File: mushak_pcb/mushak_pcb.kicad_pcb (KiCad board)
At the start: 4 copper layers, 45.8 x 40 mm, 110 parts, among them IC1 AS5600-ASOT, IC2 AS5600-ASOT, J1 Conn_01x04_Male, J10 IR_1, J11 AS5600_1, J12 IR_2, J13 AS5600_2, J14 IR_3, J15 ToF, J16 IR_4, J17 ToF, J2 Conn_01x02_Female, J3 BLE_Conn, J4 AS5600_Left, J5 AS5600_Right, J6 IR_1, J7 IR_3, J8 IR_2, J9 IR_4, M1 motor, M2 motor, Q1 DMN3065LW-7, Q2 DMN3065LW-7, Q3 DMN3065LW-7, Q4 DMN3065LW-7, Q5 DMN3065LW-7, SW1 SW_Push, SW2 SW_Push, U2 TLV1117LV30DCYT, U3 DRV8833PW, U4 VL6180XV0NR/1, U5 MPU-6500, U6 STM32F405RGTx, Y1 25Mhz, Y2 32.769kHz

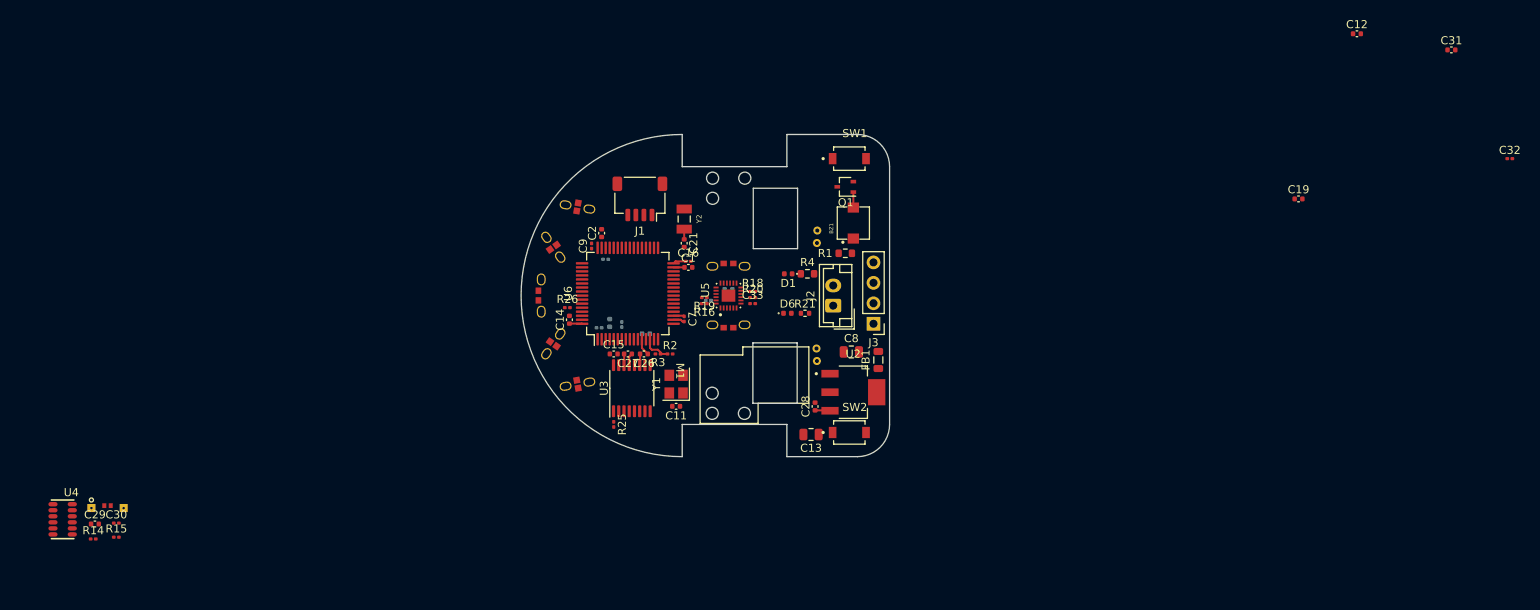
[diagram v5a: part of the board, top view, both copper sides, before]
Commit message: VL6180x part routed
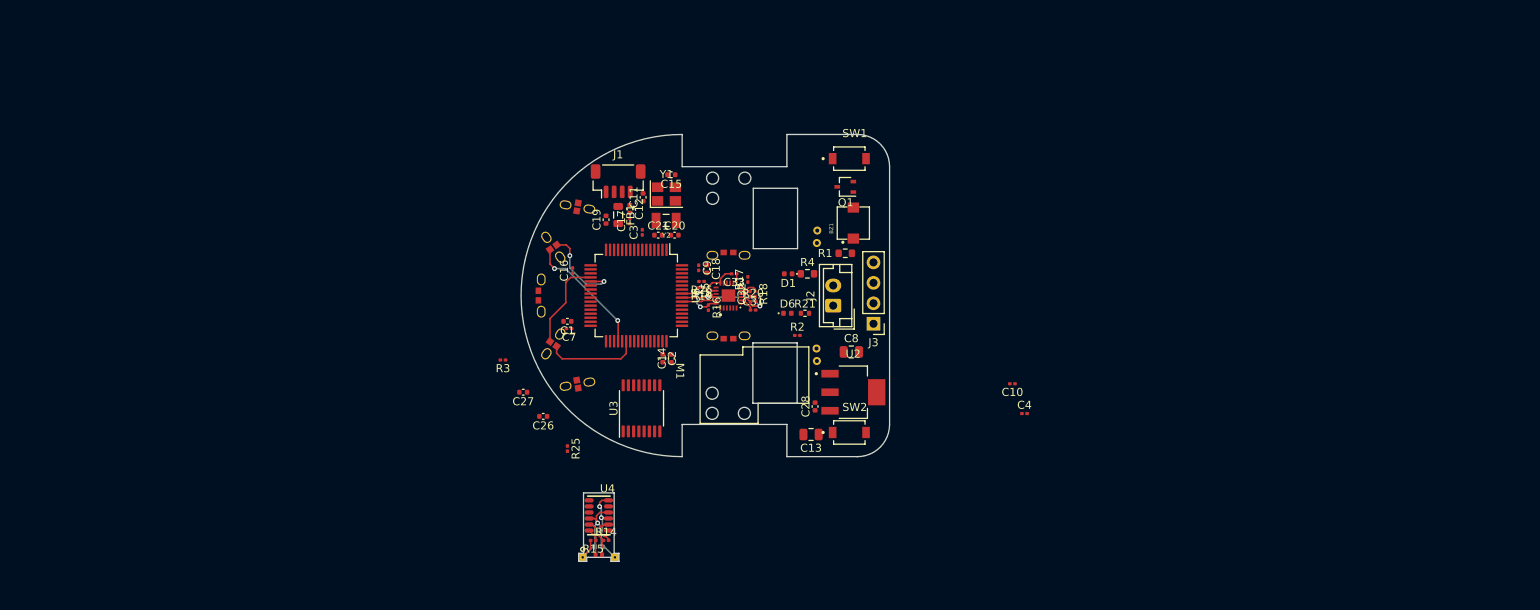
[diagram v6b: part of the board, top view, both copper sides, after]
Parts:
- C10, C18, C20, C3, C4, R17: moved to F.Cu
- C17: footprint Capacitor_SMD:C_0402_1005Metric -> Capacitor_SMD:C_0201_0603Metric; moved to F.Cu
- C29, C30: moved to B.Cu
- C31: footprint Capacitor_SMD:C_0402_1005Metric -> Capacitor_SMD:C_0201_0603Metric
- J1: footprint Connector_JST:JST_SH_SM04B-SRSS-TB_1x04-1MP_P1.00mm_Horizontal -> Connector_JST:JST_SH_BM04B-SRSS-TB_1x04-1MP_P1.00mm_Vertical
- moved C32 95.8 mm to (176.7, 96.8), turned to 90 degrees
- moved C12 92.9 mm to (161.8, 86.2), turned to -90 degrees
- moved C31 92.5 mm to (177.1, 98.8)
- moved C19 86.0 mm to (158.8, 87.6), turned to 90 degrees
- moved U4 66.6 mm to (157.9, 124.3)
- moved R14 63.7 mm to (158.8, 127.4)
- moved C29 62.6 mm to (157.9, 128.2)
- moved J17 61.3 mm to (157.9, 129.5)
- moved C30 59.9 mm to (157.9, 126.2)
- moved R15 59.2 mm to (157.2, 127.4), turned to 180 degrees
- moved C4 55.4 mm to (210.8, 111.7), turned to 0 degrees
- moved C10 51.8 mm to (209.2, 108.0), turned to 180 degrees
- moved FB1 37.0 mm to (160.3, 87.0), turned to -90 degrees
- moved C11 26.3 mm to (163.4, 84.8), turned to 90 degrees
- moved Y1 23.6 mm to (166.3, 84.4), turned to 0 degrees
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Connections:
- R14 pad 1: /VL6180x/SDA_s -> /VL6180x/SCL_s
- U4 pad 4: Net-(U4-Pad4) -> /VL6180x/3V0_s
- U4 pad 5: /VL6180x/SDA_s -> /VL6180x/SCL_s
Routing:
- net /VL6180x/3V0_s: track 0.00 -> 15.8 mm, vias 0 -> 1
- net IR_LED_3: track 0.00 -> 15.7 mm, vias 0 -> 2
- net /MPU6500/MISO: track 0.00 -> 13.2 mm, vias 0 -> 2
- net IR_LED_2: track 0.00 -> 11.6 mm
- net IR_RES_2: track 0.00 -> 11.5 mm
- net IR_RES_3: track 0.00 -> 11.1 mm, vias 0 -> 2
- net /VL6180x/GND_s: track 0.00 -> 10.2 mm, vias 0 -> 2
- net /MPU6500/MOSI: track 0.00 -> 5.88 mm, vias 0 -> 2
- net /VL6180x/SCL_s: track 0.00 -> 4.91 mm
- net /MPU6500/SCLK: track 0.00 -> 4.29 mm
- net BAT_VOL: track 3.68 -> 0.00 mm
- net /VL6180x/SDA_s: track 0.00 -> 3.37 mm
- net Net-(R18-Pad1): track 0.00 -> 2.28 mm
- net /MPU6500/nCS: track 0.00 -> 2.09 mm
- net Net-(BZ1-Pad2): track 1.92 -> 0.00 mm
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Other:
- board size 45.8 x 40 mm -> 45.8 x 53 mm
- copper layers 4 -> 2

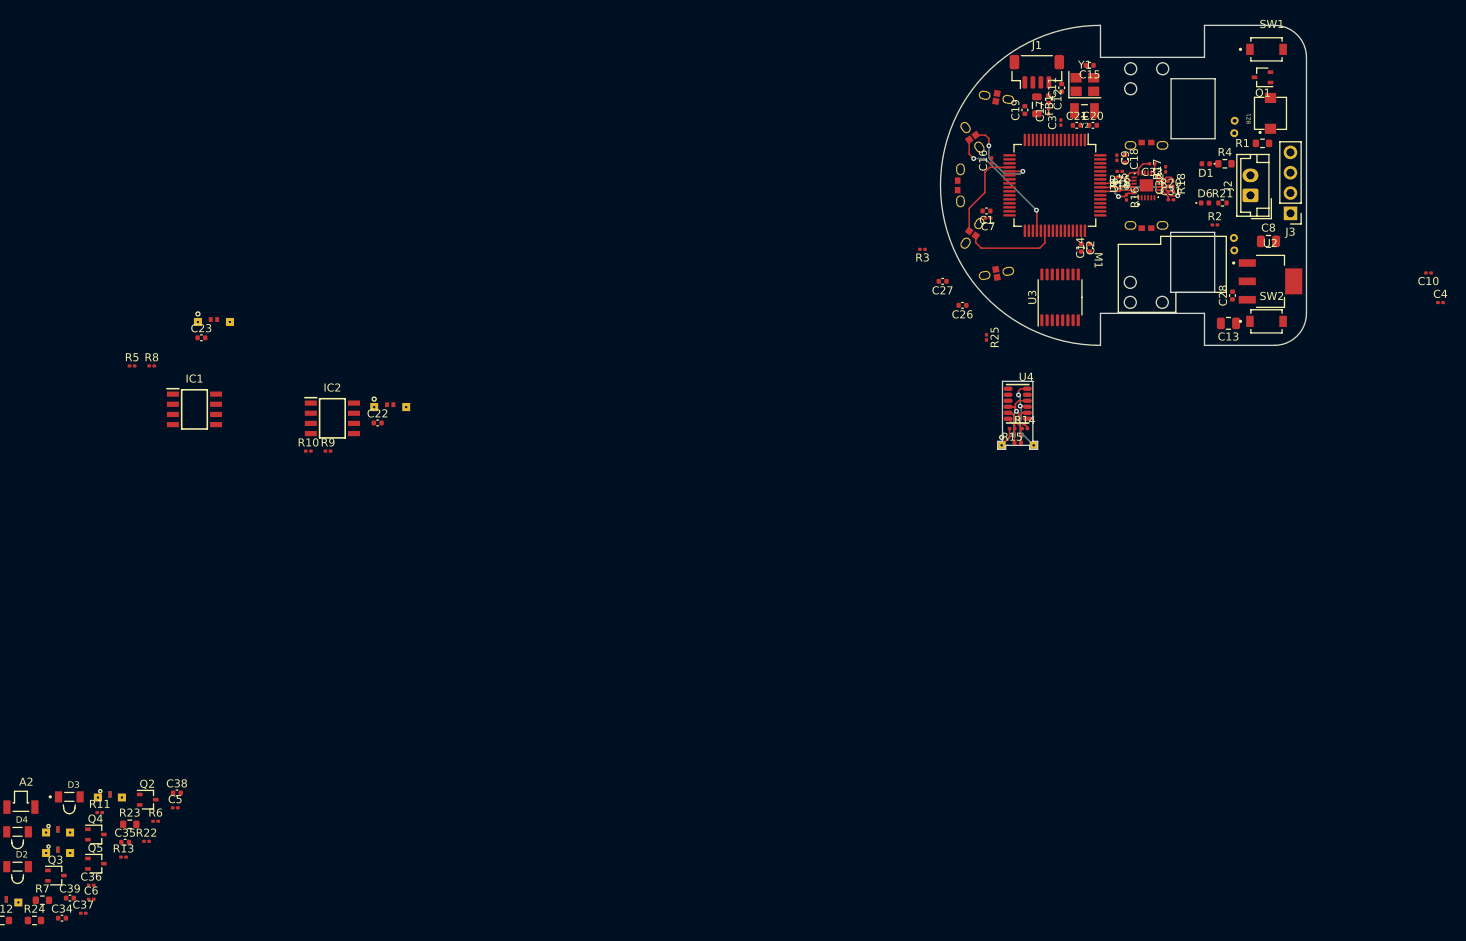
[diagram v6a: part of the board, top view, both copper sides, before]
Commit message: changed footprint of passive components
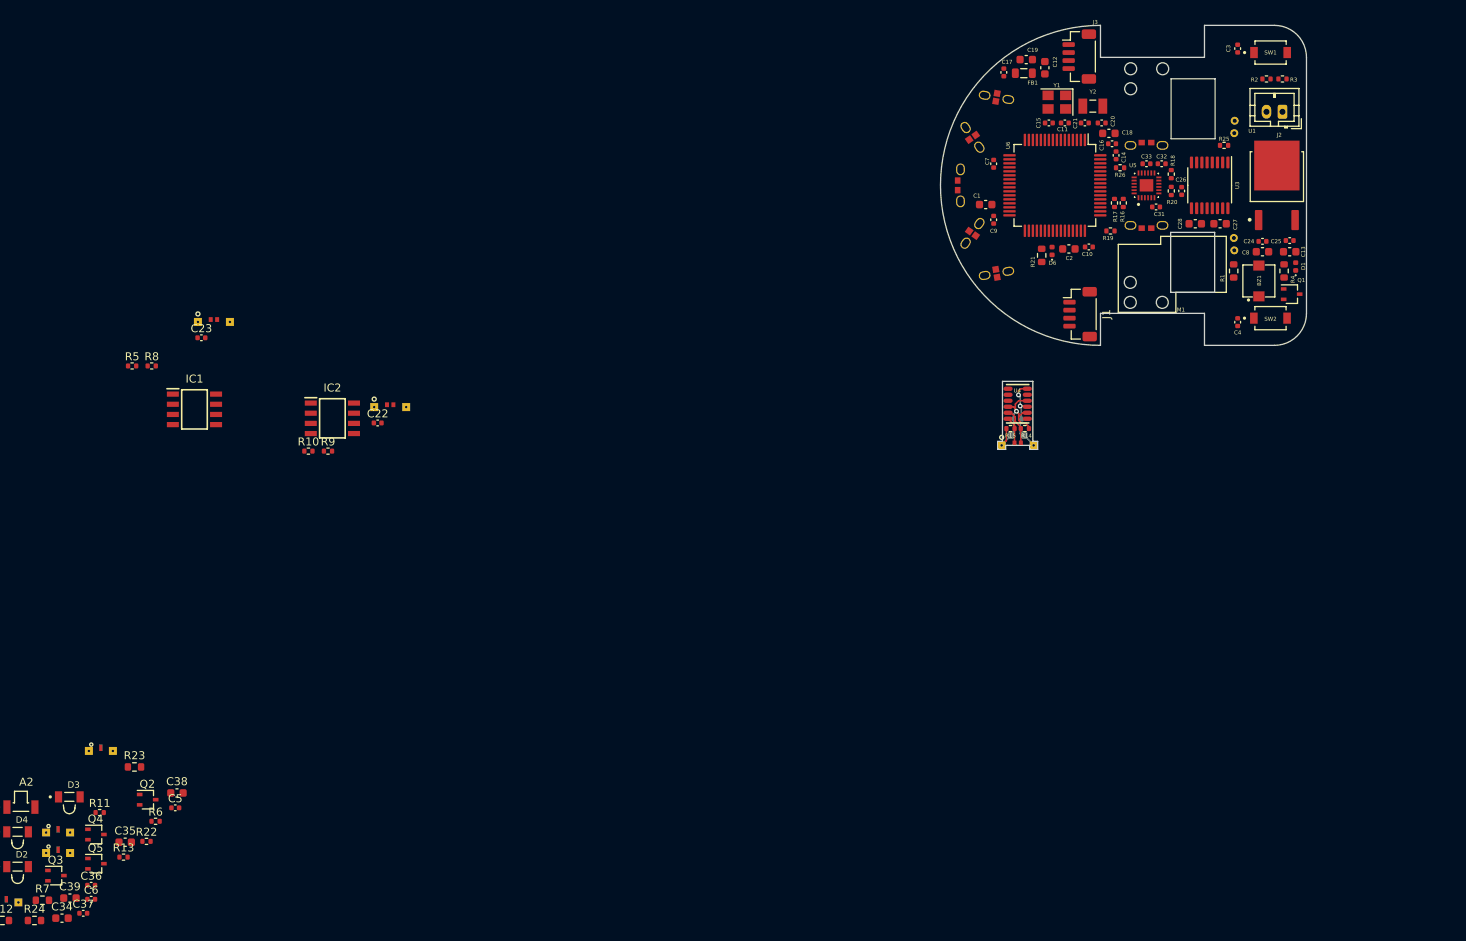
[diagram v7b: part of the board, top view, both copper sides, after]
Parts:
- removed U2: TLV1117LV30DCYT, SOT230P700X180-4N:SOT230P700X180-4N
- added C24: 0.1uF, Capacitor_SMD:C_0402_1005Metric, F.Cu at (188.5, 104.0)
- added C25: 0.1uF, Capacitor_SMD:C_0402_1005Metric, F.Cu at (191.9, 103.9)
- added U1: BA30BC0FP-E2, IPD50P04P4L-11:DPAK228P998X235-3N, F.Cu at (190.3, 97.0)
- C1, C12, C18, C19, C2, C27, C28, C29, C34, C35, C38, C39: footprint Capacitor_SMD:C_0402_1005Metric -> Capacitor_SMD:C_0603_1608Metric
- C10, C16, C17, C3, C30, C32, C33, C36, C37, C4, C5, C6, C7, C9: footprint Capacitor_SMD:C_0201_0603Metric -> Capacitor_SMD:C_0402_1005Metric
- C13: value 47uF -> 22uF; footprint Capacitor_SMD:C_0805_2012Metric -> Capacitor_SMD:C_0603_1608Metric
- C31: value 0.01uf -> 0.01uF; footprint Capacitor_SMD:C_0201_0603Metric -> Capacitor_SMD:C_0402_1005Metric
- C8: value 47uF -> 10uF; footprint Capacitor_SMD:C_0805_2012Metric -> Capacitor_SMD:C_0603_1608Metric
- J2: footprint Connector_JST:JST_EH_B2B-EH-A_1x02_P2.50mm_Vertical -> Connector_JST:JST_PH_B2B-PH-K_1x02_P2.00mm_Vertical
- J3: footprint Connector_PinHeader_2.54mm:PinHeader_1x04_P2.54mm_Vertical -> Connector_JST:JST_SH_BM04B-SRSS-TB_1x04-1MP_P1.00mm_Vertical
- R10, R11, R13, R14, R15, R16, R17, R18, R19, R20, R22, R25, R5, R6, R8, R9: footprint Resistor_SMD:R_0201_0603Metric -> Resistor_SMD:R_0402_1005Metric
- R2, R3: value 5k -> 4.7k; footprint Resistor_SMD:R_0201_0603Metric -> Resistor_SMD:R_0402_1005Metric
- R21: footprint Resistor_SMD:R_0402_1005Metric -> Resistor_SMD:R_0603_1608Metric
- R26: value 47k -> 10k; footprint Resistor_SMD:R_0201_0603Metric -> Resistor_SMD:R_0402_1005Metric
- moved R3 49.8 mm to (191.0, 83.7), turned to 0 degrees
- moved C10 42.6 mm to (166.8, 104.7), turned to 0 degrees
- moved R25 38.2 mm to (183.7, 92.0), turned to 180 degrees
- moved C27 35.4 mm to (183.2, 101.8), turned to 0 degrees
- moved J3 32.9 mm to (165.6, 80.9), turned to -90 degrees
- moved C26 30.9 mm to (178.4, 97.7), turned to -90 degrees
- moved J1 30.8 mm to (165.7, 113.1), turned to -90 degrees
- moved Q1 27.3 mm to (192.2, 110.6), turned to 0 degrees
- moved C4 25.5 mm to (185.4, 114.1), turned to -90 degrees
- moved C3 24.0 mm to (185.4, 79.9)
- moved R21 23.5 mm to (160.9, 105.8), turned to -90 degrees
- moved U3 23.4 mm to (181.9, 97.0), turned to -90 degrees
- moved BZ1 21.0 mm to (188.1, 109.0)
- moved D6 20.0 mm to (162.2, 105.2), turned to 90 degrees
- moved R2 19.4 mm to (189.0, 83.7), turned to 180 degrees
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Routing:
- net IR_LED_3: track 15.7 -> 0.00 mm, vias 2 -> 0
- net /MPU6500/MISO: track 13.2 -> 0.00 mm, vias 2 -> 0
- net IR_LED_2: track 11.6 -> 0.00 mm
- net IR_RES_2: track 11.5 -> 0.00 mm
- net IR_RES_3: track 11.1 -> 0.00 mm, vias 2 -> 0
- net POW_GND: track 6.25 -> 0.00 mm
- net /MPU6500/MOSI: track 5.88 -> 0.00 mm, vias 2 -> 0
- net /MPU6500/SCLK: track 4.29 -> 0.00 mm
- net +3V0: track 3.06 -> 0.00 mm
- net Net-(R18-Pad1): track 2.28 -> 0.00 mm
- net /MPU6500/nCS: track 2.09 -> 0.00 mm
- net Net-(C32-Pad2): track 1.29 -> 0.00 mm

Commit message: Started Poer trace routing
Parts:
- J2: footprint Connector_JST:JST_PH_B2B-PH-K_1x02_P2.00mm_Vertical -> Connector_JST:JST_SHL_SM02B-SHLS-TF_1x02-1MP_P1.00mm_Horizontal
- moved D1 17.6 mm to (187.4, 90.4), turned to 180 degrees
- moved R4 16.8 mm to (189.8, 91.0)
- moved C25 12.9 mm to (187.4, 91.8), turned to 0 degrees
- moved C24 12.7 mm to (191.9, 91.8), turned to 180 degrees
- moved C13 12.6 mm to (187.7, 93.4), turned to 0 degrees
- moved C8 12.2 mm to (191.3, 93.4), turned to 180 degrees
- moved C19 8.84 mm to (157.0, 89.9), turned to -90 degrees
- moved FB1 7.61 mm to (155.1, 89.7), turned to 90 degrees
- moved C12 7.60 mm to (168.8, 83.5), turned to -90 degrees
- moved Q1 6.50 mm to (186.0, 108.5), turned to 180 degrees
- moved C27 6.04 mm to (185.7, 96.3), turned to -90 degrees
- moved C17 4.93 mm to (157.2, 87.7), turned to 0 degrees
- moved C21 4.19 mm to (169.2, 86.2), turned to 0 degrees
- moved C28 3.90 mm to (184.0, 101.9), turned to 0 degrees
- moved R1 3.79 mm to (186.1, 111.3), turned to 0 degrees
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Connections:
- M2 pad 1: Net-(M2-Pad1) -> Net-(U3-Pad5)
- M2 pad 2: Net-(M2-Pad2) -> Net-(U3-Pad7)
- U3 pad 5: Net-(M2-Pad2) -> Net-(U3-Pad5)
- U3 pad 7: Net-(M2-Pad1) -> Net-(U3-Pad7)
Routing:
- net POW_GND: track 0.00 -> 52.8 mm, vias 0 -> 10
- net +3V0: track 0.00 -> 40.6 mm
- net POW_IN: track 0.00 -> 19.5 mm
- net TXD: track 0.00 -> 13.9 mm
- net Net-(U3-Pad2): track 0.00 -> 12.7 mm
- net RXD: track 0.00 -> 11.7 mm
- net Net-(U3-Pad4): track 0.00 -> 11.2 mm
- net Net-(C21-Pad1): track 0.00 -> 8.46 mm
- net Net-(U3-Pad7): track 0.00 -> 8.18 mm
- net RCC_OSC_IN: track 0.00 -> 6.97 mm
- net RCC_OSC_OUT: track 0.00 -> 6.08 mm
- net Net-(U3-Pad5): track 0.00 -> 5.68 mm
- net Net-(C20-Pad1): track 0.00 -> 5.27 mm
- net /MPU6500/SCLK: track 0.00 -> 5.15 mm
- net Net-(BZ1-Pad2): track 0.00 -> 4.42 mm
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- added copper zone on B.Cu, net POW_GND
- added copper zone on F.Cu, net POW_GND
